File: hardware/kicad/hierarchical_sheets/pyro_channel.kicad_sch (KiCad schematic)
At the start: 22 parts, among them J2 282834-2, J3 282834-4, U2 ZXCT1110W5-7, U3 SI9926CDY

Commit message: sync
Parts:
- R1, R10, R11, R12, R2, R4, R5, R6, R7, R8, R9: footprint Resistor_SMD:R_0402_1005Metric -> Resistor_SMD:R_0603_1608Metric
- R3: footprint Resistor_SMD:R_1206_3216Metric -> Resistor_SMD:R_0603_1608Metric
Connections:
- net CH1-.: no longer F5.2, R6.1, U3.5 (D2), U3.6 (D2)
- net CH2-.: no longer F1.2, R5.1, U3.7 (D1), U3.8 (D1)
- new net CH1-F: F5.2, R6.1, U3.5 (D2), U3.6 (D2)
- new net CH2-F: F1.2, R5.1, U3.7 (D1), U3.8 (D1)
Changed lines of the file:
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@@
     (effects (font (size 1.27 1.27)) (justify left bottom))
   )
-  (label "CH1-." (at 143.51 140.97 0) (fields_autoplaced)
+  (label "CH1-F" (at 143.51 140.97 0) (fields_autoplaced)
     (effects (font (size 1.27 1.27)) (justify left bottom))
   )
@@
     (effects (font (size 1.27 1.27)) (justify left bottom))
   )
-  (label "CH2-." (at 143.51 113.03 0) (fields_autoplaced)
+  (label "CH2-F" (at 143.51 113.03 0) (fields_autoplaced)
     (effects (font (size 1.27 1.27)) (justify left bottom))
   )
@@
       (effects (font (size 1.27 1.27)) (justify left))
     )
-    (property "Footprint" "Resistor_SMD:R_0402_1005Metric" (at 50.165 94.615 0)
+    (property "Footprint" "Resistor_SMD:R_0603_1608Metric" (at 50.165 94.615 0)
       (effects (font (size 1.27 1.27)) hide)
     )
@@
       (effects (font (size 1.27 1.27)) (justify left))
     )
-    (property "Footprint" "Resistor_SMD:R_0402_1005Metric" (at 59.055 106.045 0)
+    (property "Footprint" "Resistor_SMD:R_0603_1608Metric" (at 59.055 106.045 0)
       (effects (font (size 1.27 1.27)) hide)
     )
@@
       (effects (font (size 1.27 1.27)) (justify left))
     )
-    (property "Footprint" "Resistor_SMD:R_0402_1005Metric" (at 149.86 118.11 0)
+    (property "Footprint" "Resistor_SMD:R_0603_1608Metric" (at 149.86 118.11 0)
       (effects (font (size 1.27 1.27)) hide)
     )
@@
       (effects (font (size 1.27 1.27)) (justify left))
     )
-    (property "Footprint" "Resistor_SMD:R_0402_1005Metric" (at 236.855 121.92 0)
+    (property "Footprint" "Resistor_SMD:R_0603_1608Metric" (at 236.855 121.92 0)
       (effects (font (size 1.27 1.27)) hide)
     )
@@
       (effects (font (size 1.27 1.27)) (justify left))
     )
-    (property "Footprint" "Resistor_SMD:R_0402_1005Metric" (at 236.855 141.605 0)
+    (property "Footprint" "Resistor_SMD:R_0603_1608Metric" (at 236.855 141.605 0)
       (effects (font (size 1.27 1.27)) hide)
     )
@@
       (effects (font (size 1.27 1.27)) (justify left))
     )
-    (property "Footprint" "Resistor_SMD:R_0402_1005Metric" (at 232.41 117.475 0)
+    (property "Footprint" "Resistor_SMD:R_0603_1608Metric" (at 232.41 117.475 0)
       (effects (font (size 1.27 1.27)) hide)
     )
@@
       (effects (font (size 1.27 1.27)) (justify left))
     )
-    (property "Footprint" "Resistor_SMD:R_0402_1005Metric" (at 158.75 127 0)
+    (property "Footprint" "Resistor_SMD:R_0603_1608Metric" (at 158.75 127 0)
       (effects (font (size 1.27 1.27)) hide)
     )
@@
       (effects (font (size 1.27 1.27)) (justify left))
     )
-    (property "Footprint" "Resistor_SMD:R_0402_1005Metric" (at 232.41 137.16 0)
+    (property "Footprint" "Resistor_SMD:R_0603_1608Metric" (at 232.41 137.16 0)
       (effects (font (size 1.27 1.27)) hide)
     )
@@
       (effects (font (size 1.27 1.27)) (justify left))
     )
-    (property "Footprint" "Resistor_SMD:R_0402_1005Metric" (at 158.75 154.94 0)
+    (property "Footprint" "Resistor_SMD:R_0603_1608Metric" (at 158.75 154.94 0)
       (effects (font (size 1.27 1.27)) hide)
     )
@@
       (effects (font (size 1.27 1.27)))
     )
-    (property "Footprint" "Resistor_SMD:R_1206_3216Metric" (at 79.375 90.043 90)
+    (property "Footprint" "Resistor_SMD:R_0603_1608Metric" (at 79.375 90.043 90)
       (effects (font (size 1.27 1.27)) hide)
     )
@@
       (effects (font (size 1.27 1.27)) (justify left))
     )
-    (property "Footprint" "Resistor_SMD:R_0402_1005Metric" (at 149.86 146.05 0)
+    (property "Footprint" "Resistor_SMD:R_0603_1608Metric" (at 149.86 146.05 0)
       (effects (font (size 1.27 1.27)) hide)
     )
@@
       (effects (font (size 1.27 1.27)))
     )
-    (property "Footprint" "Resistor_SMD:R_0402_1005Metric" (at 80.137 113.665 90)
-      (effects (font (size 1.27 1.27)) hide)
-    )
+    (property "Footprint" "Resistor_SMD:R_0603_1608Metric" (at 80.137 113.665 90)
+      (effects (font (size 1.27 1.27)) hide)
+    )

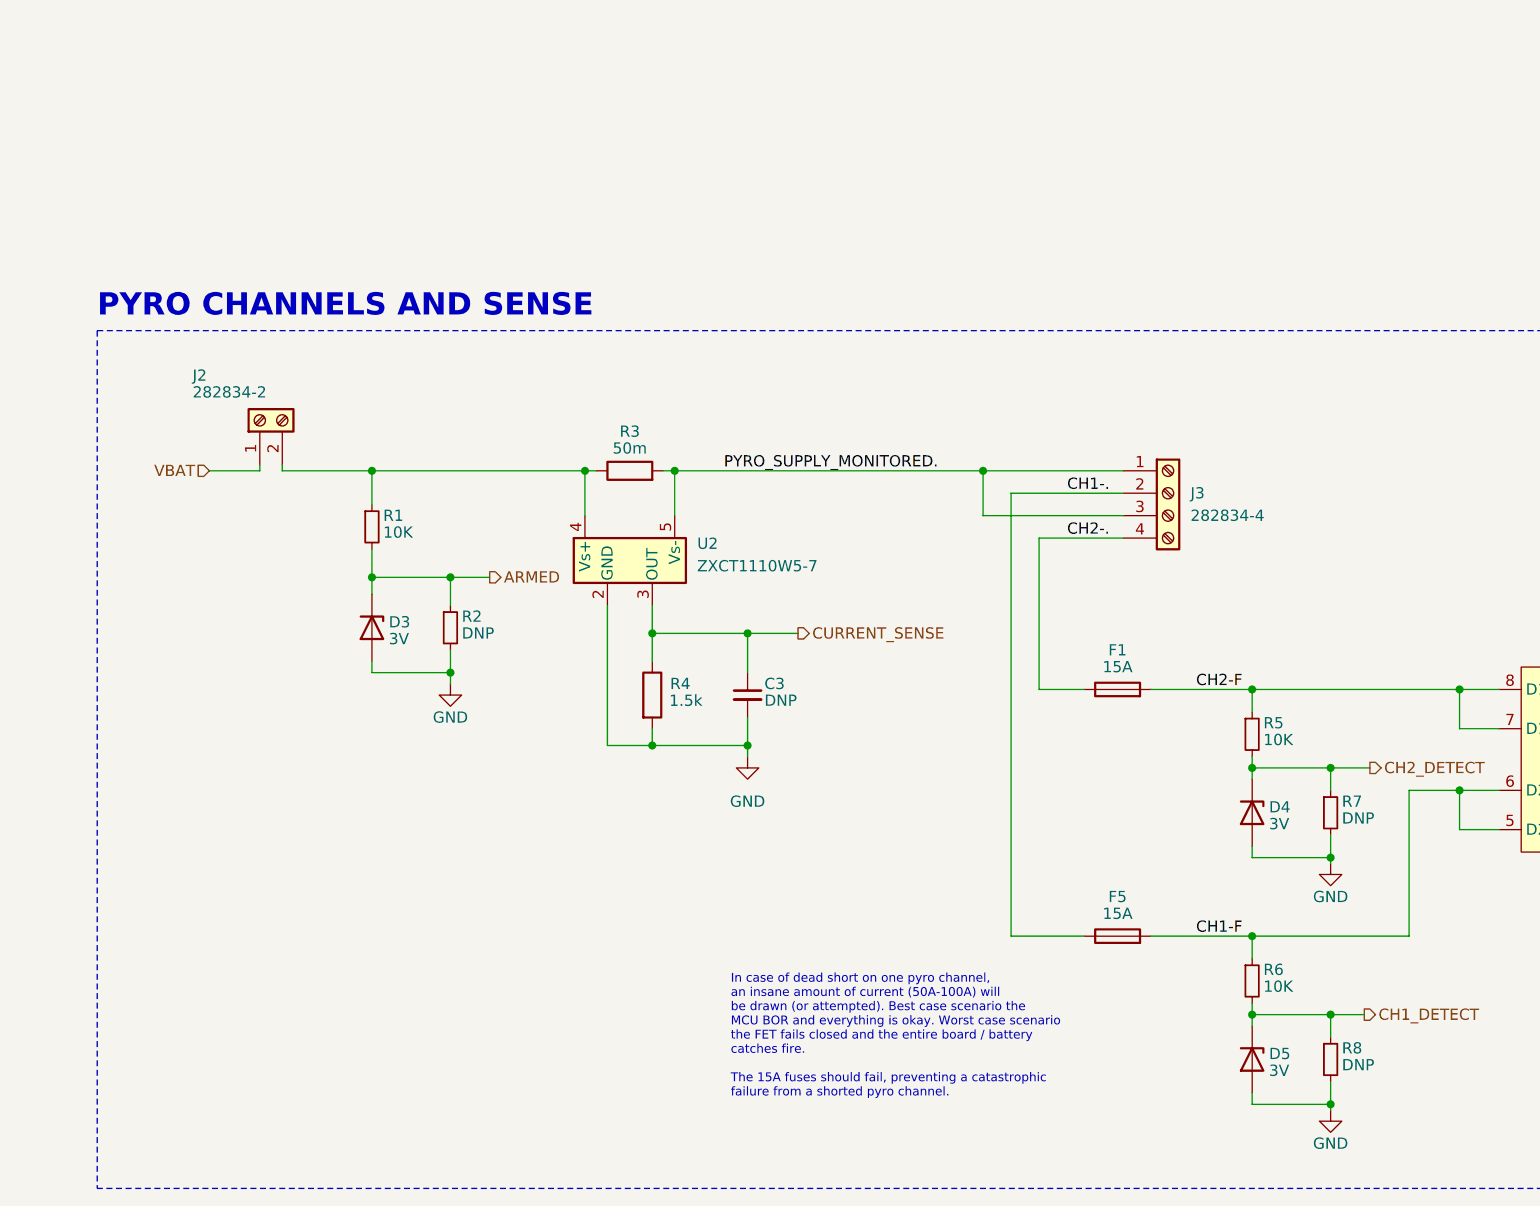
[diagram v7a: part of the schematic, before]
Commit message: added minimum fire energy thread
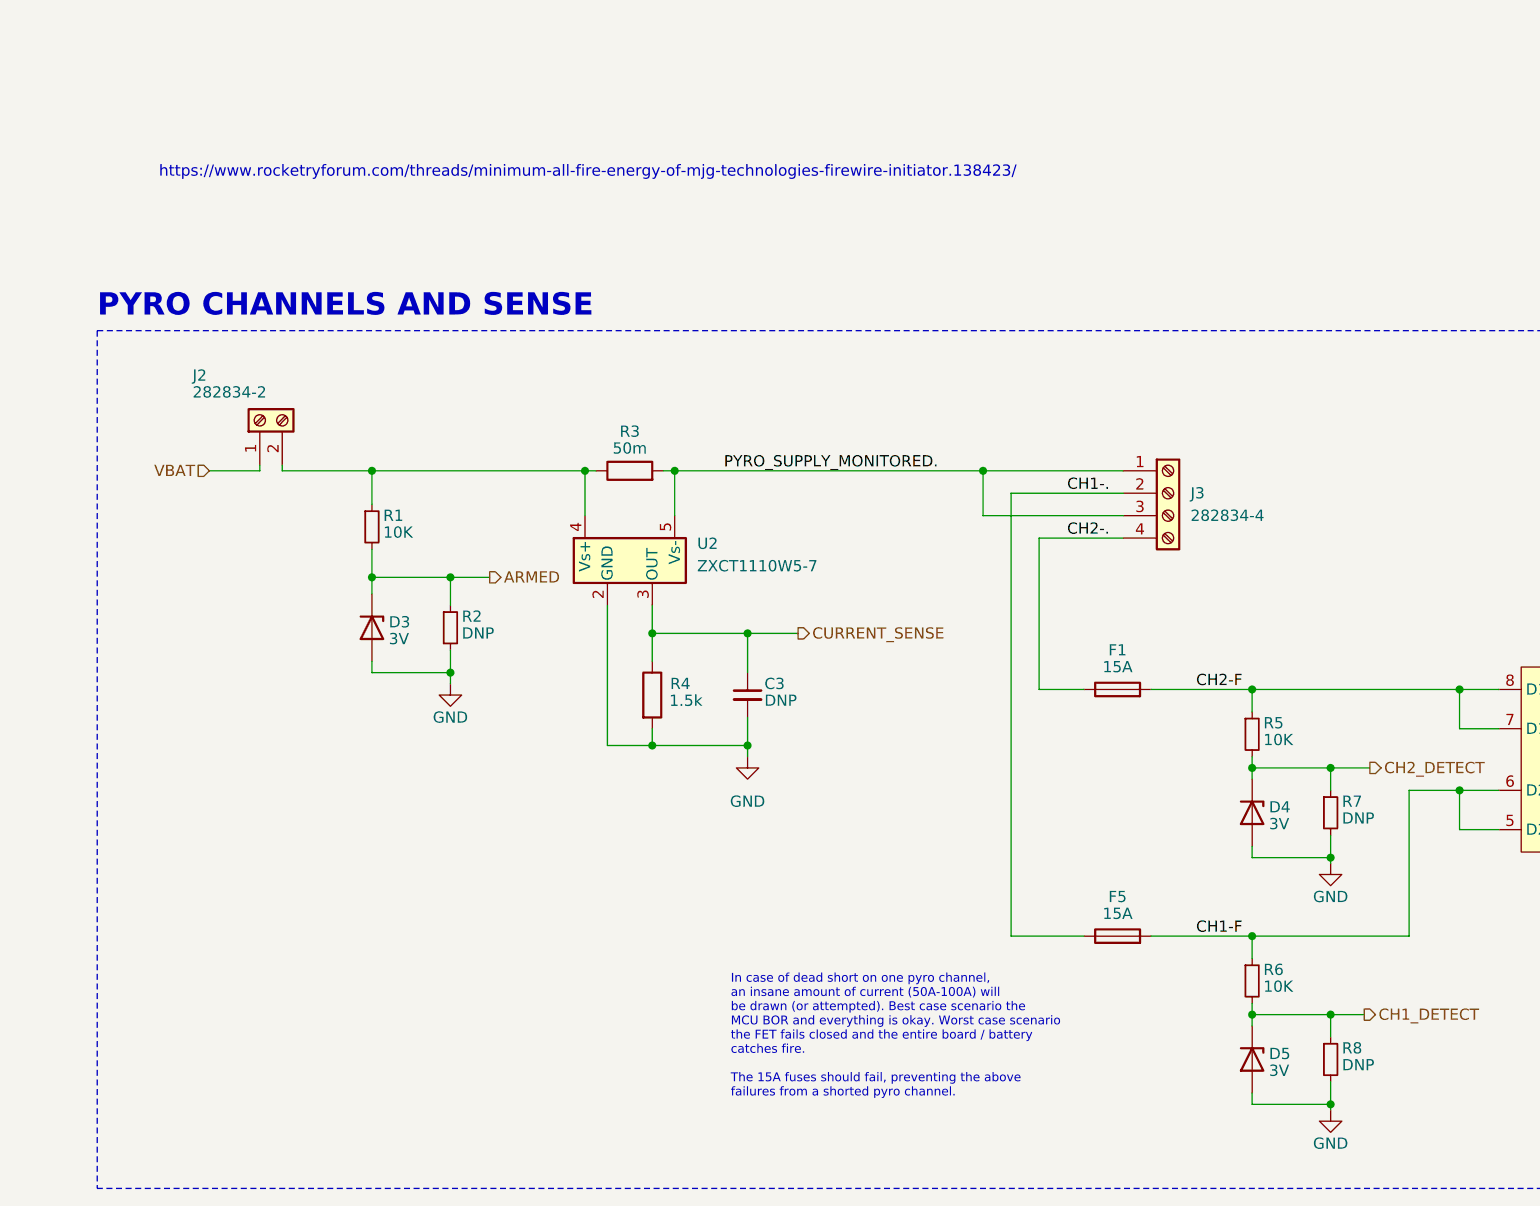
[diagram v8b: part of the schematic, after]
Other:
- note added: "In case of dead short on one pyro channel, an insane amount of current (50A-100A) will be drawn (or attempted). Best case scenario the MCU BOR and everything is okay. Worst case scenario the FET fails closed and the entire board / battery catches fire. The 15A fuses should fail, preventing the above failures from a shorted pyro channel."
- note added: "https://www.rocketryforum.com/threads/minimum-all-fire-energy-of-mjg-technologies-firewire-initiator.138423/"
- note removed: "In case of dead short on one pyro channel, an insane amount of current (50A-100A) will be drawn (or attempted). Best case scenario the MCU BOR and everything is okay. Worst case scenario the FET fails closed and the entire board / battery catches fire. The 15A fuses should fail, preventing a catastrophic failure from a shorted pyro channel."
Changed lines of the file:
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@@
+    (effects (font (size 1.27 1.27)) (justify left bottom))
+  )
+  (text "https://www.rocketryforum.com/threads/minimum-all-fire-energy-of-mjg-technologies-firewire-initiator.138423/"
+    (at 26.035 55.245 0)
     (effects (font (size 1.27 1.27)) (justify left bottom))
   )
@@
     (effects (font (size 2.52 2.52) (thickness 0.504) bold) (justify left bottom))
   )
-  (text "In case of dead short on one pyro channel, \nan insane amount of current (50A-100A) will\nbe drawn (or attempted). Best case scenario the \nMCU BOR and everything is okay. Worst case scenario\nthe FET fails closed and the entire board / battery\ncatches fire. \n\nThe 15A fuses should fail, preventing a catastrophic \nfailure from a shorted pyro channel.  "
+  (text "In case of dead short on one pyro channel, \nan insane amount of current (50A-100A) will\nbe drawn (or attempted). Best case scenario the \nMCU BOR and everything is okay. Worst case scenario\nthe FET fails closed and the entire board / battery\ncatches fire. \n\nThe 15A fuses should fail, preventing the above\nfailures from a shorted pyro channel.  "
     (at 90.805 159.385 0)
     (effects (font (size 1 1)) (justify left bottom))
